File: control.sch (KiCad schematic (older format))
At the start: 17 parts, among them IC1 ATTINY4313-P, P2 CONN_02X03, SW1 SW_Push, Y1 11.0592MHz

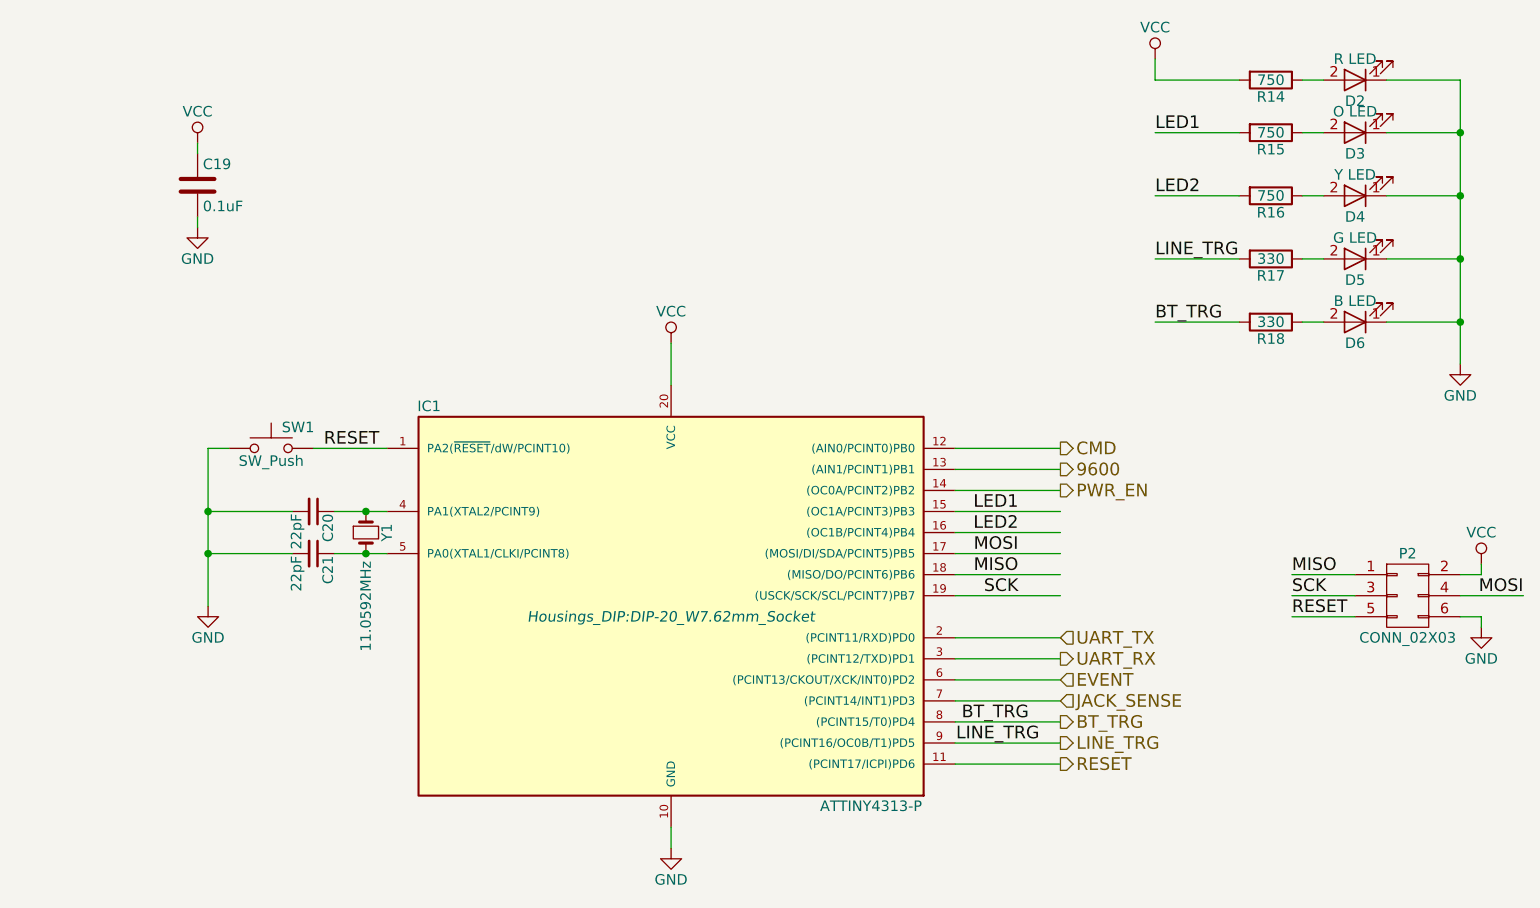
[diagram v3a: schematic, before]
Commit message: Add LEDs to BT module
These already exist on the breakout board, but they will be more visible
if I add resistors to the front panel. They can be removed if space is
limited and the case is translucent, but add them for now. In V2, there
won't be a breakout board, so adding them now makes the V1 to V2 fewer
changes.
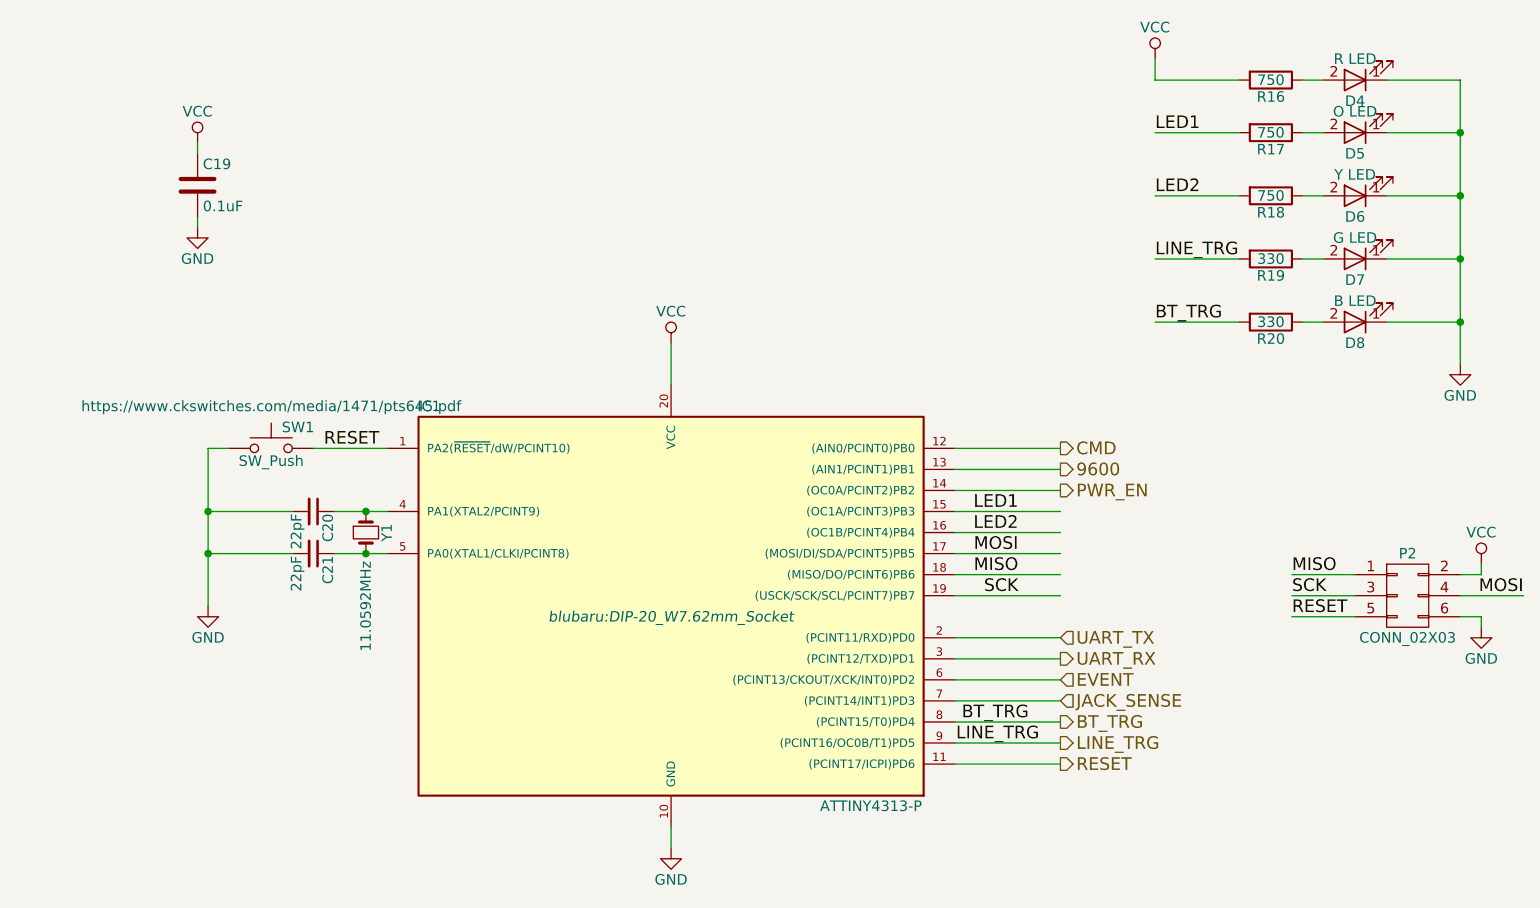
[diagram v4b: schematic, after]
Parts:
- D4: renamed from D2; footprint LEDs:LED_D3.0mm_Horizontal_O1.27mm_Z2.0mm -> LEDs:LED_D3.0mm_Horizontal_O1.27mm_Z6.0mm
- D5: renamed from D3; footprint LEDs:LED_D3.0mm_Horizontal_O1.27mm_Z2.0mm -> LEDs:LED_D3.0mm_Horizontal_O1.27mm_Z6.0mm
- D6: renamed from D4; footprint LEDs:LED_D3.0mm_Horizontal_O1.27mm_Z2.0mm -> LEDs:LED_D3.0mm_Horizontal_O1.27mm_Z6.0mm
- D7: renamed from D5; footprint LEDs:LED_D3.0mm_Horizontal_O1.27mm_Z2.0mm -> LEDs:LED_D3.0mm_Horizontal_O1.27mm_Z6.0mm
- D8: renamed from D6; footprint LEDs:LED_D3.0mm_Horizontal_O1.27mm_Z2.0mm -> LEDs:LED_D3.0mm_Horizontal_O1.27mm_Z6.0mm
- IC1: footprint Housings_DIP:DIP-20_W7.62mm_Socket -> blubaru:DIP-20_W7.62mm_Socket
- renumbered R14 to R16, R15 to R17, R16 to R18, R17 to R19, R18 to R20
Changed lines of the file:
@@
 BT_TRG
 $Comp
-L LED D4
+L LED D6
 U 1 1 59385827
 P 8200 2700
-F 0 "D4" H 8200 2800 50  0000 C CNN
+F 0 "D6" H 8200 2800 50  0000 C CNN
 F 1 "Y LED" H 8200 2600 50  0000 C CNN
-F 2 "LEDs:LED_D3.0mm_Horizontal_O1.27mm_Z2.0mm" H 8200 2700 50  0001 C CNN
+F 2 "LEDs:LED_D3.0mm_Horizontal_O1.27mm_Z6.0mm" H 8200 2700 50  0001 C CNN
 F 3 "http://www.kingbrightusa.com/images/catalog/SPEC/WP710A10LZGCK.pdf" H 8200 2700 50  0001 C CNN
 	1    8200 2700
@@
 $EndComp
 $Comp
-L R R16
+L R R18
 U 1 1 5939E4C5
 P 7800 2700
-F 0 "R16" V 7880 2700 50  0000 C CNN
+F 0 "R18" V 7880 2700 50  0000 C CNN
 F 1 "750" V 7800 2700 50  0000 C CNN
 F 2 "Resistors_THT:R_Axial_DIN0204_L3.6mm_D1.6mm_P5.08mm_Horizontal" V 7730 2700 50  0001 C CNN
@@
 	6300 5100 6800 5100
 $Comp
-L R R17
+L R R19
 U 1 1 5975727A
 P 7800 3000
-F 0 "R17" V 7880 3000 50  0000 C CNN
+F 0 "R19" V 7880 3000 50  0000 C CNN
 F 1 "330" V 7800 3000 50  0000 C CNN
 F 2 "Resistors_THT:R_Axial_DIN0204_L3.6mm_D1.6mm_P5.08mm_Horizontal" V 7730 3000 50  0001 C CNN
@@
 $EndComp
 $Comp
-L LED D5
+L LED D7
 U 1 1 5975729B
 P 8200 3000
-F 0 "D5" H 8200 3100 50  0000 C CNN
+F 0 "D7" H 8200 3100 50  0000 C CNN
 F 1 "G LED" H 8200 2900 50  0000 C CNN
-F 2 "LEDs:LED_D3.0mm_Horizontal_O1.27mm_Z2.0mm" H 8200 3000 50  0001 C CNN
+F 2 "LEDs:LED_D3.0mm_Horizontal_O1.27mm_Z6.0mm" H 8200 3000 50  0001 C CNN
 F 3 "http://www.kingbrightusa.com/images/catalog/SPEC/WP710A10LVBC-D.pdf" H 8200 3000 50  0001 C CNN
 	1    8200 3000
@@
 $EndComp
 $Comp
-L GND #PWR038
+L GND #PWR039
 U 1 1 597572DC
 P 8700 3500
-F 0 "#PWR038" H 8700 3250 50  0001 C CNN
+F 0 "#PWR039" H 8700 3250 50  0001 C CNN
 F 1 "GND" H 8700 3350 50  0000 C CNN
 F 2 "" H 8700 3500 50  0001 C CNN
@@
 F 0 "IC1" H 3800 5700 50  0000 C CNN
 F 1 "ATTINY4313-P" H 5900 3800 50  0000 C CNN
-F 2 "Housings_DIP:DIP-20_W7.62mm_Socket" H 4950 4700 50  0000 C CIN
+F 2 "blubaru:DIP-20_W7.62mm_Socket" H 4950 4700 50  0000 C CIN
 F 3 "http://www.atmel.com/images/doc8246.pdf" H 4950 4700 50  0001 C CNN
 F 4 "http://www.assmann-wsw.com/fileadmin/datasheets/ASS_0810_CO.pdf" H 4950 4700 60  0001 C CNN "Socket"
@@
 Connection ~ 2750 4400
 $Comp
-L GND #PWR039
+L GND #PWR040
 U 1 1 59F295BF
 P 2750 4650
-F 0 "#PWR039" H 2750 4400 50  0001 C CNN
+F 0 "#PWR040" H 2750 4400 50  0001 C CNN
 F 1 "GND" H 2750 4500 50  0000 C CNN
 F 2 "" H 2750 4650 50  0000 C CNN
@@
 $EndComp
 $Comp
-L GND #PWR040
+L GND #PWR041
 U 1 1 59F295E5
 P 4950 5800
-F 0 "#PWR040" H 4950 5550 50  0001 C CNN
+F 0 "#PWR041" H 4950 5550 50  0001 C CNN
 F 1 "GND" H 4950 5650 50  0000 C CNN
 F 2 "" H 4950 5800 50  0000 C CNN
@@
 	4950 5700 4950 5800
 $Comp
-L VCC #PWR041
+L VCC #PWR042
 U 1 1 59F29632
 P 4950 3400
-F 0 "#PWR041" H 4950 3250 50  0001 C CNN
+F 0 "#PWR042" H 4950 3250 50  0001 C CNN
 F 1 "VCC" H 4950 3550 50  0000 C CNN
 F 2 "" H 4950 3400 50  0000 C CNN
@@
 F 1 "SW_Push" H 3050 3840 50  0000 C CNN
 F 2 "Buttons_Switches_THT:SW_Tactile_SPST_Angled_PTS645Vx58-2LFS" H 3050 4100 50  0001 C CNN
-F 3 "" H 3050 4100 50  0000 C CNN
+F 3 "https://www.ckswitches.com/media/1471/pts645.pdf" H 3050 4100 50  0000 C CNN
 	1    3050 3900
 	1    0    0    -1
@@
 	2700 2500 2700 2450
 $Comp
-L GND #PWR042
+L GND #PWR043
 U 1 1 59F2A079
 P 2700 2850
-F 0 "#PWR042" H 2700 2600 50  0001 C CNN
+F 0 "#PWR043" H 2700 2600 50  0001 C CNN
 F 1 "GND" H 2700 2700 50  0000 C CNN
 F 2 "" H 2700 2850 50  0000 C CNN
@@
 $EndComp
 $Comp
-L VCC #PWR043
+L VCC #PWR044
 U 1 1 59F2A6EF
 P 8800 4450
-F 0 "#PWR043" H 8800 4300 50  0001 C CNN
+F 0 "#PWR044" H 8800 4300 50  0001 C CNN
 F 1 "VCC" H 8800 4600 50  0000 C CNN
 F 2 "" H 8800 4450 50  0000 C CNN
@@
 $EndComp
 $Comp
-L GND #PWR044
+L GND #PWR045
 U 1 1 59F2A72F
 P 8800 4750
-F 0 "#PWR044" H 8800 4500 50  0001 C CNN
+F 0 "#PWR045" H 8800 4500 50  0001 C CNN
 F 1 "GND" H 8800 4600 50  0000 C CNN
 F 2 "" H 8800 4750 50  0000 C CNN
@@
 MOSI
 $Comp
-L LED D6
+L LED D8
 U 1 1 59F2C4A1
 P 8200 3300
-F 0 "D6" H 8200 3400 50  0000 C CNN
+F 0 "D8" H 8200 3400 50  0000 C CNN
 F 1 "B LED" H 8200 3200 50  0000 C CNN
-F 2 "LEDs:LED_D3.0mm_Horizontal_O1.27mm_Z2.0mm" H 8200 3300 50  0001 C CNN
+F 2 "LEDs:LED_D3.0mm_Horizontal_O1.27mm_Z6.0mm" H 8200 3300 50  0001 C CNN
 F 3 "http://www.kingbrightusa.com/images/catalog/SPEC/WP710A10LVBC-D.pdf" H 8200 3300 50  0001 C CNN
 	1    8200 3300
@@
 $EndComp
 $Comp
-L LED D3
+L LED D5
 U 1 1 59F2C6B4
 P 8200 2400
-F 0 "D3" H 8200 2500 50  0000 C CNN
+F 0 "D5" H 8200 2500 50  0000 C CNN
 F 1 "O LED" H 8200 2300 50  0000 C CNN
-F 2 "LEDs:LED_D3.0mm_Horizontal_O1.27mm_Z2.0mm" H 8200 2400 50  0001 C CNN
+F 2 "LEDs:LED_D3.0mm_Horizontal_O1.27mm_Z6.0mm" H 8200 2400 50  0001 C CNN
 F 3 "http://www.kingbrightusa.com/images/catalog/SPEC/WP710A10LSECK-J4.pdf" H 8200 2400 50  0001 C CNN
 	1    8200 2400
@@
 $EndComp
 $Comp
-L R R18
+L R R20
 U 1 1 59F2C711
 P 7800 3300
-F 0 "R18" V 7880 3300 50  0000 C CNN
+F 0 "R20" V 7880 3300 50  0000 C CNN
 F 1 "330" V 7800 3300 50  0000 C CNN
 F 2 "Resistors_THT:R_Axial_DIN0204_L3.6mm_D1.6mm_P5.08mm_Horizontal" V 7730 3300 50  0001 C CNN
@@
 $EndComp
 $Comp
-L R R15
+L R R17
 U 1 1 59F2C754
 P 7800 2400
-F 0 "R15" V 7880 2400 50  0000 C CNN
+F 0 "R17" V 7880 2400 50  0000 C CNN
 F 1 "750" V 7800 2400 50  0000 C CNN
 F 2 "Resistors_THT:R_Axial_DIN0204_L3.6mm_D1.6mm_P5.08mm_Horizontal" V 7730 2400 50  0001 C CNN
@@
 $EndComp
 $Comp
-L R R14
+L R R16
 U 1 1 59F2C832
 P 7800 2150
-F 0 "R14" V 7880 2150 50  0000 C CNN
+F 0 "R16" V 7880 2150 50  0000 C CNN
 F 1 "750" V 7800 2150 50  0000 C CNN
 F 2 "Resistors_THT:R_Axial_DIN0204_L3.6mm_D1.6mm_P5.08mm_Horizontal" V 7730 2150 50  0001 C CNN
@@
 $EndComp
 $Comp
-L LED D2
+L LED D4
 U 1 1 59F2C86B
 P 8200 2150
-F 0 "D2" H 8200 2250 50  0000 C CNN
+F 0 "D4" H 8200 2250 50  0000 C CNN
 F 1 "R LED" H 8200 2050 50  0000 C CNN
-F 2 "LEDs:LED_D3.0mm_Horizontal_O1.27mm_Z2.0mm" H 8200 2150 50  0001 C CNN
+F 2 "LEDs:LED_D3.0mm_Horizontal_O1.27mm_Z6.0mm" H 8200 2150 50  0001 C CNN
 F 3 "http://www.kingbrightusa.com/images/catalog/SPEC/WP710A10LSECK-J3.pdf" H 8200 2150 50  0001 C CNN
 	1    8200 2150
@@
 	7650 3300 7250 3300
 $Comp
-L VCC #PWR045
+L VCC #PWR046
 U 1 1 59F2CDFF
 P 7250 2050
-F 0 "#PWR045" H 7250 1900 50  0001 C CNN
+F 0 "#PWR046" H 7250 1900 50  0001 C CNN
 F 1 "VCC" H 7250 2200 50  0000 C CNN
 F 2 "" H 7250 2050 50  0000 C CNN
@@
 LED2
 $Comp
-L VCC #PWR046
+L VCC #PWR047
 U 1 1 59F2D1EA
 P 2700 2450
-F 0 "#PWR046" H 2700 2300 50  0001 C CNN
+F 0 "#PWR047" H 2700 2300 50  0001 C CNN
 F 1 "VCC" H 2700 2600 50  0000 C CNN
 F 2 "" H 2700 2450 50  0000 C CNN

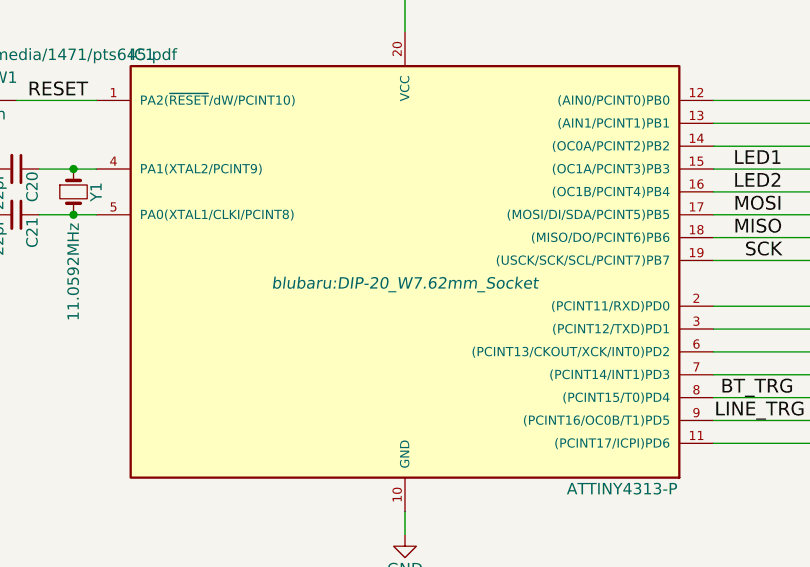
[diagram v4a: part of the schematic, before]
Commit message: Add footprints for LEDs and tactile switches
Also create an initial layout for fun.
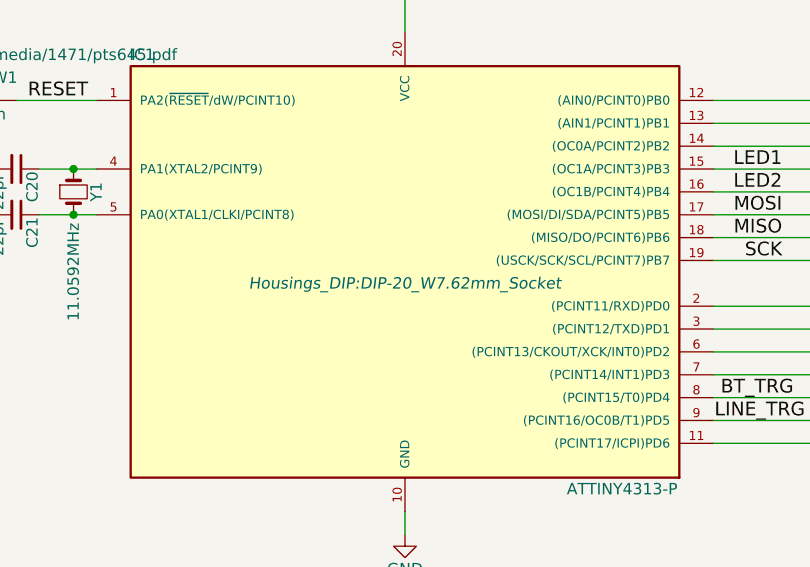
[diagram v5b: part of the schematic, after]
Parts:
- D4, D5, D7, D8: footprint LEDs:LED_D3.0mm_Horizontal_O1.27mm_Z6.0mm -> blubaru:LED_D3.0mm_Horizontal_O1.27mm_Z6.0mm; Holder datasheet (none) -> https://www.bivar.com/portals/0/products/H-10XC-X.pdf
- D6: footprint LEDs:LED_D3.0mm_Horizontal_O1.27mm_Z6.0mm -> blubaru:LED_D3.0mm_Horizontal_O1.27mm_Z6.0mm; holder datasheet (none) -> https://www.bivar.com/portals/0/products/H-10XC-X.pdf
- IC1: footprint blubaru:DIP-20_W7.62mm_Socket -> Housings_DIP:DIP-20_W7.62mm_Socket
- SW1: footprint Buttons_Switches_THT:SW_Tactile_SPST_Angled_PTS645Vx58-2LFS -> blubaru:SW_Tactile_SPST_Angled_PTS645Vx58-2LFS
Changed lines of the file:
@@
 F 0 "D6" H 8200 2800 50  0000 C CNN
 F 1 "Y LED" H 8200 2600 50  0000 C CNN
-F 2 "LEDs:LED_D3.0mm_Horizontal_O1.27mm_Z6.0mm" H 8200 2700 50  0001 C CNN
+F 2 "blubaru:LED_D3.0mm_Horizontal_O1.27mm_Z6.0mm" H 8200 2700 50  0001 C CNN
 F 3 "http://www.kingbrightusa.com/images/catalog/SPEC/WP710A10LZGCK.pdf" H 8200 2700 50  0001 C CNN
+F 4 "https://www.bivar.com/portals/0/products/H-10XC-X.pdf" H 8200 2700 60  0001 C CNN "holder datasheet"
 	1    8200 2700
 	-1   0    0    1
@@
 F 0 "D7" H 8200 3100 50  0000 C CNN
 F 1 "G LED" H 8200 2900 50  0000 C CNN
-F 2 "LEDs:LED_D3.0mm_Horizontal_O1.27mm_Z6.0mm" H 8200 3000 50  0001 C CNN
+F 2 "blubaru:LED_D3.0mm_Horizontal_O1.27mm_Z6.0mm" H 8200 3000 50  0001 C CNN
 F 3 "http://www.kingbrightusa.com/images/catalog/SPEC/WP710A10LVBC-D.pdf" H 8200 3000 50  0001 C CNN
+F 4 "https://www.bivar.com/portals/0/products/H-10XC-X.pdf" H 8200 3000 60  0001 C CNN "Holder datasheet"
 	1    8200 3000
 	-1   0    0    1
@@
 F 0 "IC1" H 3800 5700 50  0000 C CNN
 F 1 "ATTINY4313-P" H 5900 3800 50  0000 C CNN
-F 2 "blubaru:DIP-20_W7.62mm_Socket" H 4950 4700 50  0000 C CIN
+F 2 "Housings_DIP:DIP-20_W7.62mm_Socket" H 4950 4700 50  0000 C CIN
 F 3 "http://www.atmel.com/images/doc8246.pdf" H 4950 4700 50  0001 C CNN
 F 4 "http://www.assmann-wsw.com/fileadmin/datasheets/ASS_0810_CO.pdf" H 4950 4700 60  0001 C CNN "Socket"
@@
 F 0 "SW1" H 3100 4000 50  0000 L CNN
 F 1 "SW_Push" H 3050 3840 50  0000 C CNN
-F 2 "Buttons_Switches_THT:SW_Tactile_SPST_Angled_PTS645Vx58-2LFS" H 3050 4100 50  0001 C CNN
+F 2 "blubaru:SW_Tactile_SPST_Angled_PTS645Vx58-2LFS" H 3050 4100 50  0001 C CNN
 F 3 "https://www.ckswitches.com/media/1471/pts645.pdf" H 3050 4100 50  0000 C CNN
 	1    3050 3900
@@
 F 0 "D8" H 8200 3400 50  0000 C CNN
 F 1 "B LED" H 8200 3200 50  0000 C CNN
-F 2 "LEDs:LED_D3.0mm_Horizontal_O1.27mm_Z6.0mm" H 8200 3300 50  0001 C CNN
+F 2 "blubaru:LED_D3.0mm_Horizontal_O1.27mm_Z6.0mm" H 8200 3300 50  0001 C CNN
 F 3 "http://www.kingbrightusa.com/images/catalog/SPEC/WP710A10LVBC-D.pdf" H 8200 3300 50  0001 C CNN
+F 4 "https://www.bivar.com/portals/0/products/H-10XC-X.pdf" H 8200 3300 60  0001 C CNN "Holder datasheet"
 	1    8200 3300
 	-1   0    0    1
@@
 F 0 "D5" H 8200 2500 50  0000 C CNN
 F 1 "O LED" H 8200 2300 50  0000 C CNN
-F 2 "LEDs:LED_D3.0mm_Horizontal_O1.27mm_Z6.0mm" H 8200 2400 50  0001 C CNN
+F 2 "blubaru:LED_D3.0mm_Horizontal_O1.27mm_Z6.0mm" H 8200 2400 50  0001 C CNN
 F 3 "http://www.kingbrightusa.com/images/catalog/SPEC/WP710A10LSECK-J4.pdf" H 8200 2400 50  0001 C CNN
+F 4 "https://www.bivar.com/portals/0/products/H-10XC-X.pdf" H 8200 2400 60  0001 C CNN "Holder datasheet"
 	1    8200 2400
 	-1   0    0    1
@@
 F 0 "D4" H 8200 2250 50  0000 C CNN
 F 1 "R LED" H 8200 2050 50  0000 C CNN
-F 2 "LEDs:LED_D3.0mm_Horizontal_O1.27mm_Z6.0mm" H 8200 2150 50  0001 C CNN
+F 2 "blubaru:LED_D3.0mm_Horizontal_O1.27mm_Z6.0mm" H 8200 2150 50  0001 C CNN
 F 3 "http://www.kingbrightusa.com/images/catalog/SPEC/WP710A10LSECK-J3.pdf" H 8200 2150 50  0001 C CNN
+F 4 "https://www.bivar.com/portals/0/products/H-10XC-X.pdf" H 8200 2150 60  0001 C CNN "Holder datasheet"
 	1    8200 2150
 	-1   0    0    1

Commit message: Re-add MCU footprint and use vertical regul.
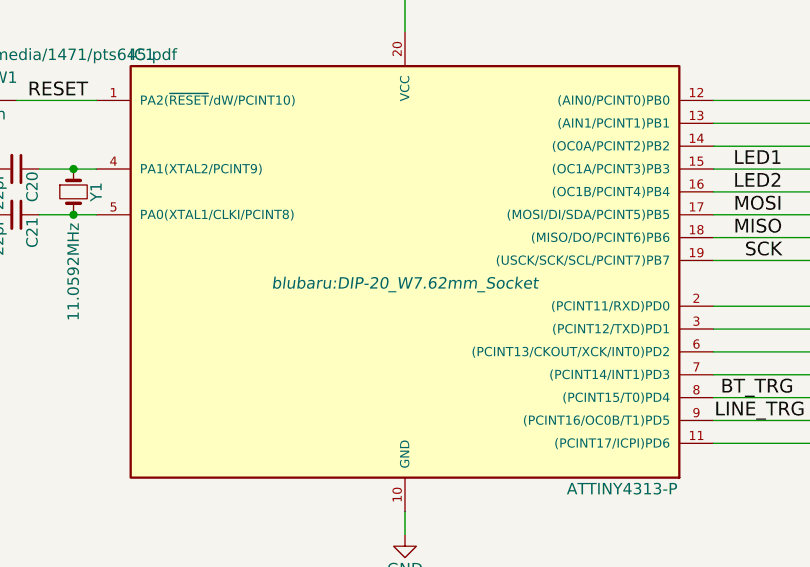
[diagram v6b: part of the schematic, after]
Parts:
- IC1: footprint Housings_DIP:DIP-20_W7.62mm_Socket -> blubaru:DIP-20_W7.62mm_Socket
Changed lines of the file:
@@
 F 0 "IC1" H 3800 5700 50  0000 C CNN
 F 1 "ATTINY4313-P" H 5900 3800 50  0000 C CNN
-F 2 "Housings_DIP:DIP-20_W7.62mm_Socket" H 4950 4700 50  0000 C CIN
+F 2 "blubaru:DIP-20_W7.62mm_Socket" H 4950 4700 50  0000 C CIN
 F 3 "http://www.atmel.com/images/doc8246.pdf" H 4950 4700 50  0001 C CNN
 F 4 "http://www.assmann-wsw.com/fileadmin/datasheets/ASS_0810_CO.pdf" H 4950 4700 60  0001 C CNN "Socket"
